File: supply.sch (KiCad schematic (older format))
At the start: 74 parts, among them IC1 TPS54561, IC2 NCP380HMUAJAATBG, J10 61300311121, J3 DC_SOCKET, Q1 BC817W, U4 TPS65296, U5 TPS62823DLCT

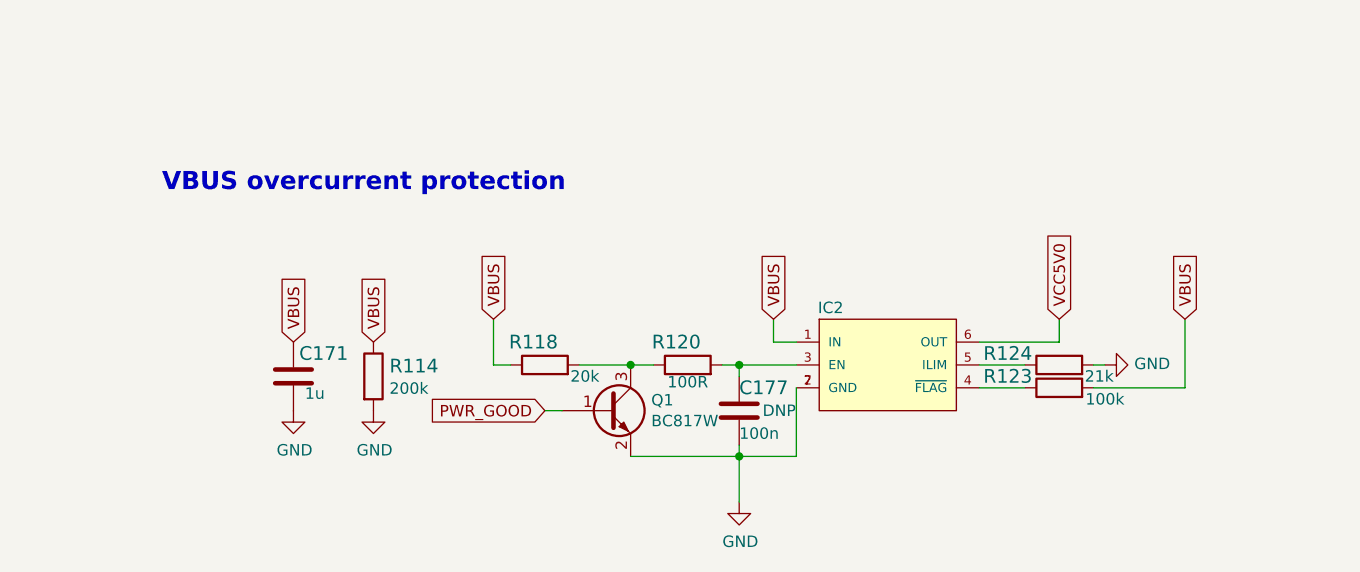
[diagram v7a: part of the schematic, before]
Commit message: Remove VBUS overcurrent protector
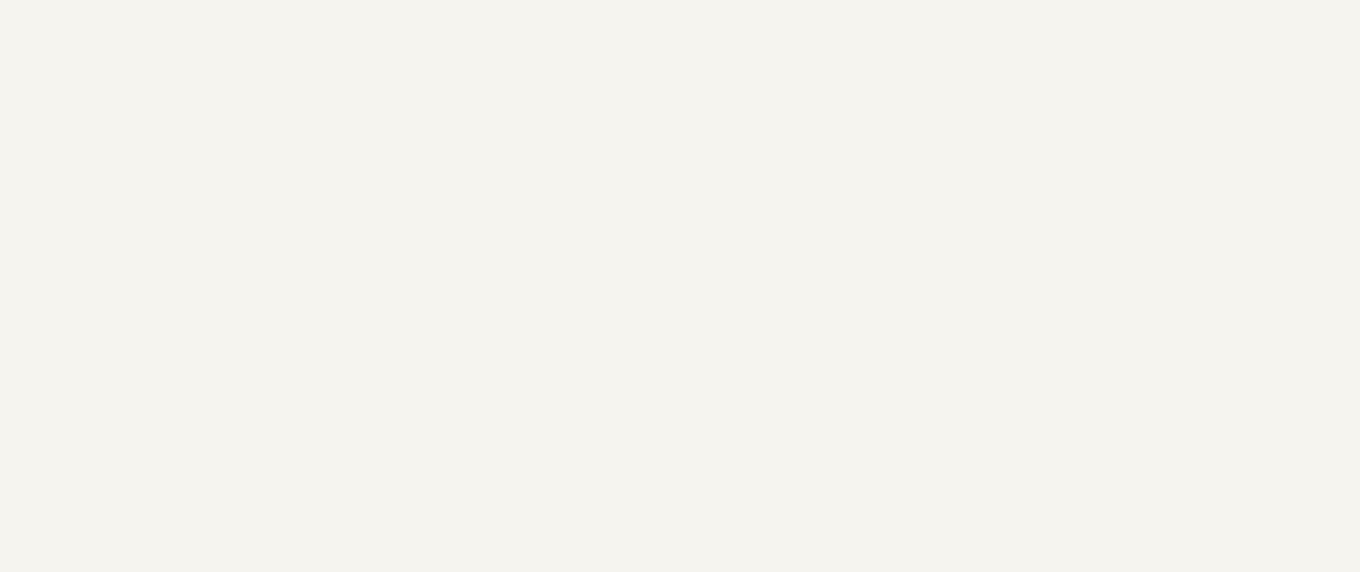
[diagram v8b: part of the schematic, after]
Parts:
- removed C171: C_1u_0402, lpddr4-test-board-footprints:0402-cap, symbol lpddr4-test-board:C_1u_0402
- removed C177: C_100n_0402_6V3, lpddr4-test-board-footprints:0402-cap, symbol lpddr4-test-board:C_100n_0402_6V3
- removed IC2: NCP380HMUAJAATBG, lpddr4-test-board-footprints:TRANS_NTLUS3A18PZTAG, symbol lpddr4-test-board:NCP380HMUAJAATBG
- removed Q1: BC817W, lpddr4-test-board-footprints:SOT-323, symbol lpddr4-test-board:BC817W
- removed R114: R_200k_0402, lpddr4-test-board-footprints:0402-res, symbol lpddr4-test-board:R_200k_0402
- removed R118: R_20k_0402, lpddr4-test-board-footprints:0402-res, symbol lpddr4-test-board:R_20k_0402
- removed R120: R_100R_0402, lpddr4-test-board-footprints:0402-res, symbol lpddr4-test-board:R_100R_0402
- removed R123: R_100k_0402, lpddr4-test-board-footprints:0402-res, symbol lpddr4-test-board:R_100k_0402
- removed R124: R_21k_0402, lpddr4-test-board-footprints:0402-res, symbol lpddr4-test-board:R_21k_0402
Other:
- note removed: "VBUS overcurrent protection"
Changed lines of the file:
@@
 	0    1    1    0
 $EndComp
-Wire Wire Line
-	5525 9250 5625 9250
-$Comp
-L lpddr4-test-board:BC817W Q1
-U 1 1 5FBC69EE
-P 5425 9450
-F 0 "Q1" H 5615 9496 50  0000 L CNN
-F 1 "BC817W" H 5615 9405 50  0000 L CNN
-F 2 "lpddr4-test-board-footprints:SOT-323" H 5625 9375 50  0001 L CIN
-F 3 "" H 5425 9450 50  0001 L CNN
-	1    5425 9450
-	1    0    0    -1
-$EndComp
-Connection ~ 5525 9250
-Wire Wire Line
-	5300 9250 5525 9250
-Wire Wire Line
-	5150 9450 5225 9450
-Wire Wire Line
-	5525 9650 6000 9650
-Wire Wire Line
-	7250 9350 7050 9350
-Wire Wire Line
-	7600 9250 7550 9250
-$Comp
-L lpddr4-test-board:C_100n_0402_6V3 C177
-U 1 1 5FD5C77D
-P 6000 9450
-F 0 "C177" H 6000 9550 60  0000 L CNN
-F 1 "C_100n_0402_6V3" H 6000 9300 60  0001 C CNN
-F 2 "lpddr4-test-board-footprints:0402-cap" H 6200 9650 60  0001 L CNN
-F 3 "" H 6000 9450 50  0001 C CNN
-F 4 "Walsin" H 6200 9850 60  0001 L CNN "Manufacturer"
-F 5 "0402X104K6R3CT" H 6200 9750 60  0001 L CNN "MPN"
-F 6 "100n" H 6000 9350 50  0000 L CNN "Val"
-F 7 "DNP" H 6175 9450 50  0000 C CNN "Populate"
-	1    6000 9450
-	1    0    0    -1
-$EndComp
-Text Notes 3475 8500 0    79   ~ 16
-VBUS overcurrent protection
-$Comp
-L lpddr4-test-board:R_21k_0402 R124
-U 1 1 61ABE48A
-P 7400 9250
-F 0 "R124" H 7175 9300 60  0000 C CNN
-F 1 "R_21k_0402" H 7400 9100 60  0001 C CNN
-F 2 "lpddr4-test-board-footprints:0402-res" H 7600 9450 60  0001 L CNN
-F 3 "" H 7400 9250 50  0001 C CNN
-F 4 "MULTICOMP PRO" H 7600 9650 60  0001 L CNN "Manufacturer"
-F 5 "MCWR04X2102FTL" H 7600 9550 60  0001 L CNN "MPN"
-F 6 "21k" H 7575 9200 50  0000 C CNN "Val"
-	1    7400 9250
-	1    0    0    -1
-$EndComp
-Text GLabel 5150 9450 0    50   Input ~ 0
-PWR_GOOD
-Wire Wire Line
-	4925 9050 4925 9250
-Wire Wire Line
-	6150 9150 6250 9150
-Wire Wire Line
-	6150 9050 6150 9150
-Wire Wire Line
-	7950 9350 7550 9350
-Wire Wire Line
-	7950 9050 7950 9350
-Wire Wire Line
-	7400 9050 7400 9150
-Text GLabel 7400 9050 1    50   Input ~ 0
-VCC5V0
-$Comp
-L lpddr4-test-board:GND #PWR0182
-U 1 1 602A9306
-P 4400 9450
-F 0 "#PWR0182" H 4400 9200 50  0001 C CNN
-F 1 "GND" H 4405 9277 50  0000 C CNN
-F 2 "" H 4400 9450 50  0001 C CNN
-F 3 "" H 4400 9450 50  0001 C CNN
-	1    4400 9450
-	1    0    0    -1
-$EndComp
-$Comp
-L lpddr4-test-board:GND #PWR0181
-U 1 1 602A9077
-P 4050 9450
-F 0 "#PWR0181" H 4050 9200 50  0001 C CNN
-F 1 "GND" H 4055 9277 50  0000 C CNN
-F 2 "" H 4050 9450 50  0001 C CNN
-F 3 "" H 4050 9450 50  0001 C CNN
-	1    4050 9450
-	1    0    0    -1
-$EndComp
-Text GLabel 4400 9150 1    50   Input ~ 0
-VBUS
-Text GLabel 4050 9150 1    50   Input ~ 0
-VBUS
-$Comp
-L lpddr4-test-board:C_1u_0402 C171
-U 1 1 602A87AE
-P 4050 9300
-F 0 "C171" H 4075 9400 60  0000 L CNN
-F 1 "C_1u_0402" H 4050 9150 60  0001 C CNN
-F 2 "lpddr4-test-board-footprints:0402-cap" H 4250 9500 60  0001 L CNN
-F 3 "" H 4050 9300 50  0001 C CNN
-F 4 "TDK" H 4250 9700 60  0001 L CNN "Manufacturer"
-F 5 "C1005X6S1A105K050BC" H 4250 9600 60  0001 L CNN "MPN"
-F 6 "1u" H 4100 9225 50  0000 L CNN "Val"
-	1    4050 9300
-	1    0    0    -1
-$EndComp
-$Comp
-L lpddr4-test-board:R_200k_0402 R114
-U 1 1 602A7F74
-P 4400 9300
-F 0 "R114" V 4355 9370 60  0000 L CNN
-F 1 "R_200k_0402" H 4400 9150 60  0001 C CNN
-F 2 "lpddr4-test-board-footprints:0402-res" H 4600 9500 60  0001 L CNN
-F 3 "" H 4400 9300 50  0001 C CNN
-F 4 "YAGEO_(PHYCOMP)" H 4600 9700 60  0001 L CNN "Manufacturer"
-F 5 "RC0402FR-07200KL" H 4600 9600 60  0001 L CNN "MPN"
-F 6 "200k" V 4453 9370 50  0000 L CNN "Val"
-	1    4400 9300
-	0    1    1    0
-$EndComp
-Text GLabel 7950 9050 1    50   Input ~ 0
-VBUS
-$Comp
-L lpddr4-test-board:R_100k_0402 R123
-U 1 1 6018960F
-P 7400 9350
-F 0 "R123" H 7175 9400 60  0000 C CNN
-F 1 "R_100k_0402" H 7400 9200 60  0001 C CNN
-F 2 "lpddr4-test-board-footprints:0402-res" H 7600 9550 60  0001 L CNN
-F 3 "" H 7400 9350 50  0001 C CNN
-F 4 "VISHAY" H 7600 9750 60  0001 L CNN "Manufacturer"
-F 5 "CRCW0402100KFKEDHP" H 7600 9650 60  0001 L CNN "MPN"
-F 6 "100k" H 7600 9300 50  0000 C CNN "Val"
-	1    7400 9350
-	1    0    0    -1
-$EndComp
-Wire Wire Line
-	6000 9250 6250 9250
-Wire Wire Line
-	6000 9300 6000 9250
-Wire Wire Line
-	6000 9650 6000 9600
-Wire Wire Line
-	6250 9350 6250 9650
-Connection ~ 6000 9650
-Wire Wire Line
-	6250 9650 6000 9650
-Wire Wire Line
-	6000 9850 6000 9650
-$Comp
-L lpddr4-test-board:GND #PWR0175
-U 1 1 6016F95A
-P 6000 9850
-F 0 "#PWR0175" H 6000 9600 50  0001 C CNN
-F 1 "GND" H 6005 9677 50  0000 C CNN
-F 2 "" H 6000 9850 50  0001 C CNN
-F 3 "" H 6000 9850 50  0001 C CNN
-	1    6000 9850
-	1    0    0    -1
-$EndComp
-Wire Wire Line
-	4925 9250 5000 9250
-Connection ~ 6000 9250
-Wire Wire Line
-	5925 9250 6000 9250
-Text GLabel 4925 9050 1    50   Input ~ 0
-VBUS
-$Comp
-L lpddr4-test-board:R_20k_0402 R118
-U 1 1 60154EC4
-P 5150 9250
-F 0 "R118" H 5100 9350 60  0000 C CNN
-F 1 "R_20k_0402" H 5150 9100 60  0001 C CNN
-F 2 "lpddr4-test-board-footprints:0402-res" H 5350 9450 60  0001 L CNN
-F 3 "" H 5150 9250 50  0001 C CNN
-F 4 "VISHAY" H 5350 9650 60  0001 L CNN "Manufacturer"
-F 5 "CRCW040220K0FKED" H 5350 9550 60  0001 L CNN "MPN"
-F 6 "20k" H 5325 9200 50  0000 C CNN "Val"
-	1    5150 9250
-	1    0    0    -1
-$EndComp
-$Comp
-L lpddr4-test-board:R_100R_0402 R120
-U 1 1 60154A15
-P 5775 9250
-F 0 "R120" H 5725 9350 60  0000 C CNN
-F 1 "R_100R_0402" H 5775 9100 60  0001 C CNN
-F 2 "lpddr4-test-board-footprints:0402-res" H 5975 9450 60  0001 L CNN
-F 3 "" H 5775 9250 50  0001 C CNN
-F 4 "BOURNS" H 5975 9650 60  0001 L CNN "Manufacturer"
-F 5 "CR0402-FX-1000GLF" H 5975 9550 60  0001 L CNN "MPN"
-F 6 "100R" H 5775 9175 50  0000 C CNN "Val"
-	1    5775 9250
-	1    0    0    -1
-$EndComp
-Text GLabel 6150 9050 1    50   Input ~ 0
-VBUS
-$Comp
-L lpddr4-test-board:GND #PWR0174
-U 1 1 60153C31
-P 7600 9250
-F 0 "#PWR0174" H 7600 9000 50  0001 C CNN
-F 1 "GND" V 7605 9122 50  0000 R CNN
-F 2 "" H 7600 9250 50  0001 C CNN
-F 3 "" H 7600 9250 50  0001 C CNN
-	1    7600 9250
-	0    -1   -1   0
-$EndComp
-Wire Wire Line
-	7050 9250 7250 9250
-Wire Wire Line
-	7050 9150 7400 9150
-$Comp
-L lpddr4-test-board:NCP380HMUAJAATBG IC2
-U 1 1 601481EA
-P 6650 9250
-F 0 "IC2" H 6400 9500 50  0000 C CNN
-F 1 "NCP380HMUAJAATBG" H 6650 9550 50  0001 L BNN
-F 2 "lpddr4-test-board-footprints:TRANS_NTLUS3A18PZTAG" H 6650 9500 50  0001 L BNN
-F 3 "" H 6800 8950 50  0001 L BNN
-	1    6650 9250
-	1    0    0    -1
-$EndComp
 $EndSCHEMATC
